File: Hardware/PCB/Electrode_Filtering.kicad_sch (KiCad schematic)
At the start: 8 parts

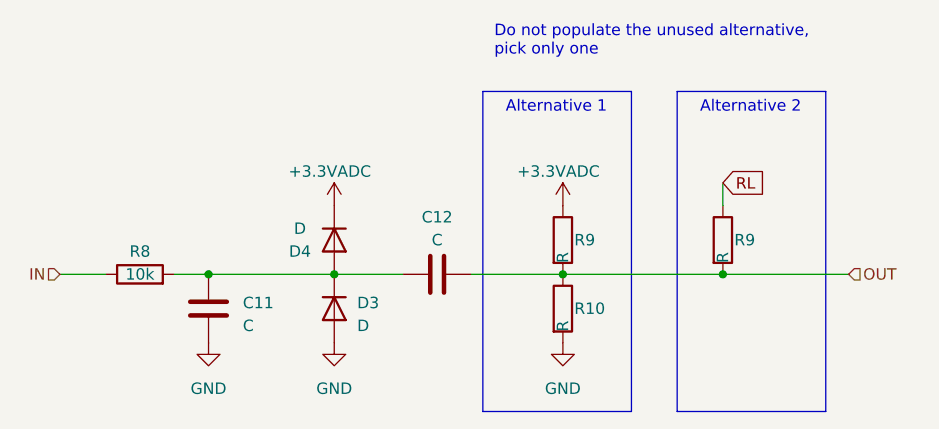
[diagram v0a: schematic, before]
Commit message: First working version, with 12-lead recording
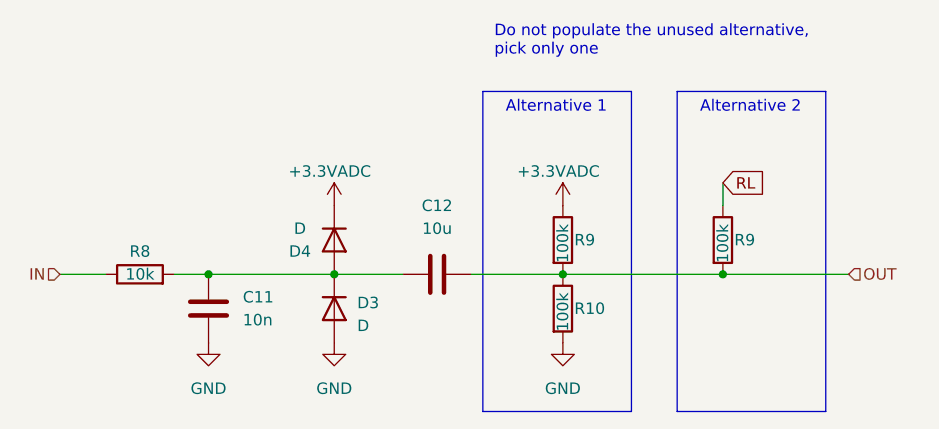
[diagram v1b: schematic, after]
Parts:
- C11: value C -> 10n
- C12: value C -> 10u
- R10, R9: value R -> 100k
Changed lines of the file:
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@@
   )
   (polyline (pts (xy 168.91 104.14) (xy 168.91 68.58))
-    (stroke (width 0) (type default))
+    (stroke (width 0) (type default) (color 132 132 132 1))
   )
   (wire (pts (xy 179.07 78.74) (xy 179.07 81.28))
@@
   )
   (polyline (pts (xy 152.4 104.14) (xy 168.91 104.14))
-    (stroke (width 0) (type default))
+    (stroke (width 0) (type default) (color 132 132 132 1))
   )
   (polyline (pts (xy 173.99 68.58) (xy 173.99 104.14))
@@
   )
   (polyline (pts (xy 152.4 68.58) (xy 168.91 68.58))
-    (stroke (width 0) (type default))
+    (stroke (width 0) (type default) (color 132 132 132 1))
   )
   (wire (pts (xy 151.13 88.9) (xy 161.29 88.9))
@@
   )
   (polyline (pts (xy 152.4 68.58) (xy 152.4 104.14))
-    (stroke (width 0) (type default))
+    (stroke (width 0) (type default) (color 132 132 132 1))
   )
   (text "Alternative 1" (at 154.94 71.12 0)
-    (effects (font (size 1.27 1.27)) (justify left bottom))
+    (effects (font (size 1.27 1.27) (color 72 72 72 1)) (justify left bottom))
   )
   (text "Alternative 2" (at 176.53 71.12 0)
@@
       (effects (font (size 1.27 1.27)) (justify left))
     )
-    (property "Value" "R" (at 179.07 87.63 90)
+    (property "Value" "100k" (at 179.07 87.63 90)
       (effects (font (size 1.27 1.27)) (justify left))
     )
@@
   (symbol (lib_id "Device:C") (at 147.32 88.9 90) (unit 1)
     (in_bom yes) (on_board yes) (dnp no) (fields_autoplaced)
-    (property "Reference" "C12" (at 147.32 82.55 90)
-      (effects (font (size 1.27 1.27)))
-    )
-    (property "Value" "C" (at 147.32 85.09 90)
+    (property "Reference" "C12" (at 147.32 81.28 90)
+      (effects (font (size 1.27 1.27)))
+    )
+    (property "Value" "10u" (at 147.32 83.82 90)
       (effects (font (size 1.27 1.27)))
     )
@@
   (symbol (lib_id "Device:C") (at 121.92 92.71 0) (unit 1)
     (in_bom yes) (on_board yes) (dnp no) (fields_autoplaced)
-    (property "Reference" "C11" (at 125.73 92.075 0)
-      (effects (font (size 1.27 1.27)) (justify left))
-    )
-    (property "Value" "C" (at 125.73 94.615 0)
+    (property "Reference" "C11" (at 125.73 91.44 0)
+      (effects (font (size 1.27 1.27)) (justify left))
+    )
+    (property "Value" "10n" (at 125.73 93.98 0)
       (effects (font (size 1.27 1.27)) (justify left))
     )
@@
       (effects (font (size 1.27 1.27)) (justify left))
     )
-    (property "Value" "R" (at 161.29 95.25 90)
+    (property "Value" "100k" (at 161.29 95.25 90)
       (effects (font (size 1.27 1.27)) (justify left))
     )
@@
       (effects (font (size 1.27 1.27)) (justify left))
     )
-    (property "Value" "R" (at 161.29 87.63 90)
-      (effects (font (size 1.27 1.27)) (justify left))
-    )
+    (property "Value" "100k" (at 161.29 87.63 90)
+      (effects (font (size 1.27 1.27)) (justify left))
+    )
